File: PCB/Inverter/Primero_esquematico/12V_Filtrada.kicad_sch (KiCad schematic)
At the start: 11 parts, among them U1 TPS259621DDAT

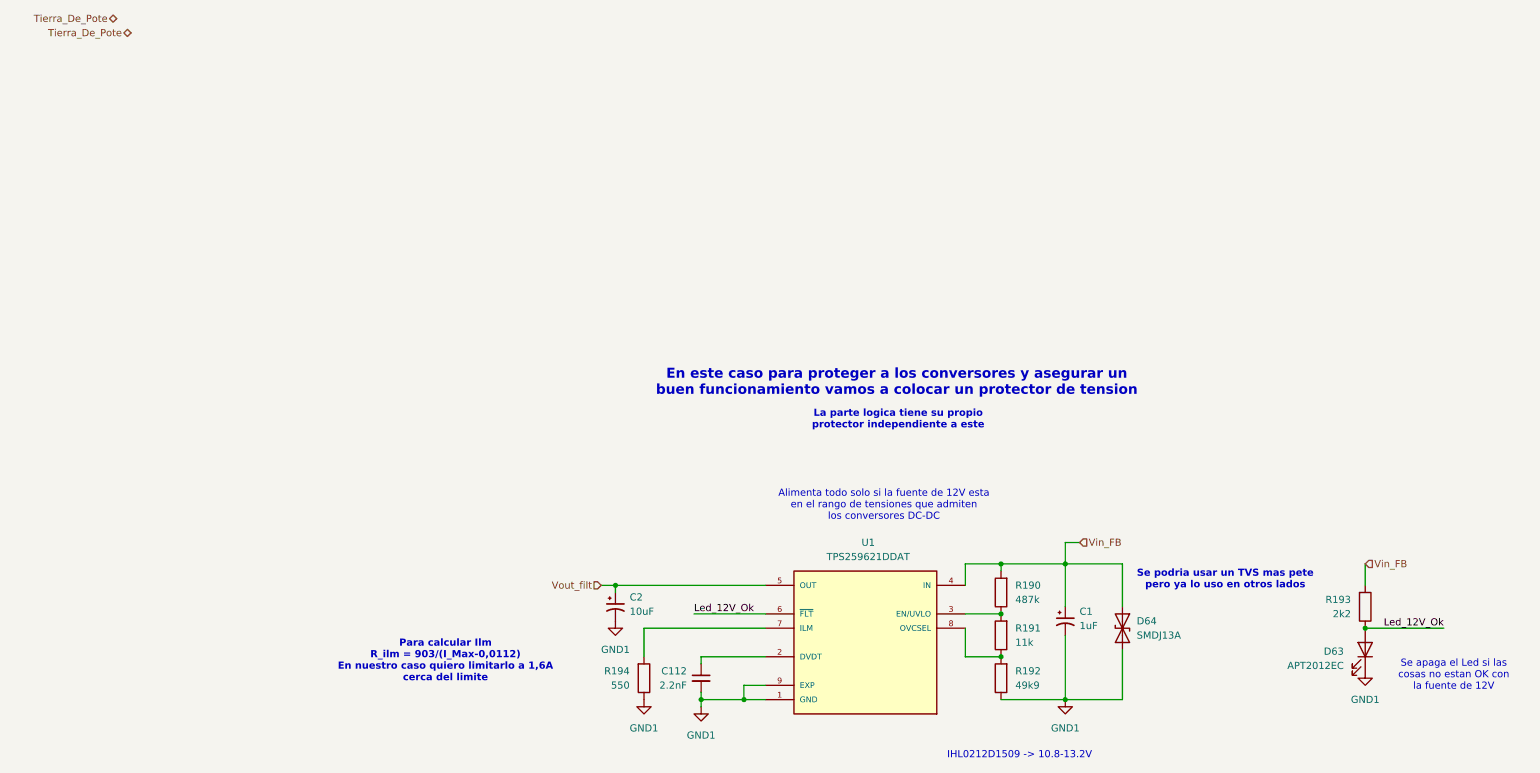
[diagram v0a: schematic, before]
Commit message: Un par de cosas q corregi del ERC pero sigue mal
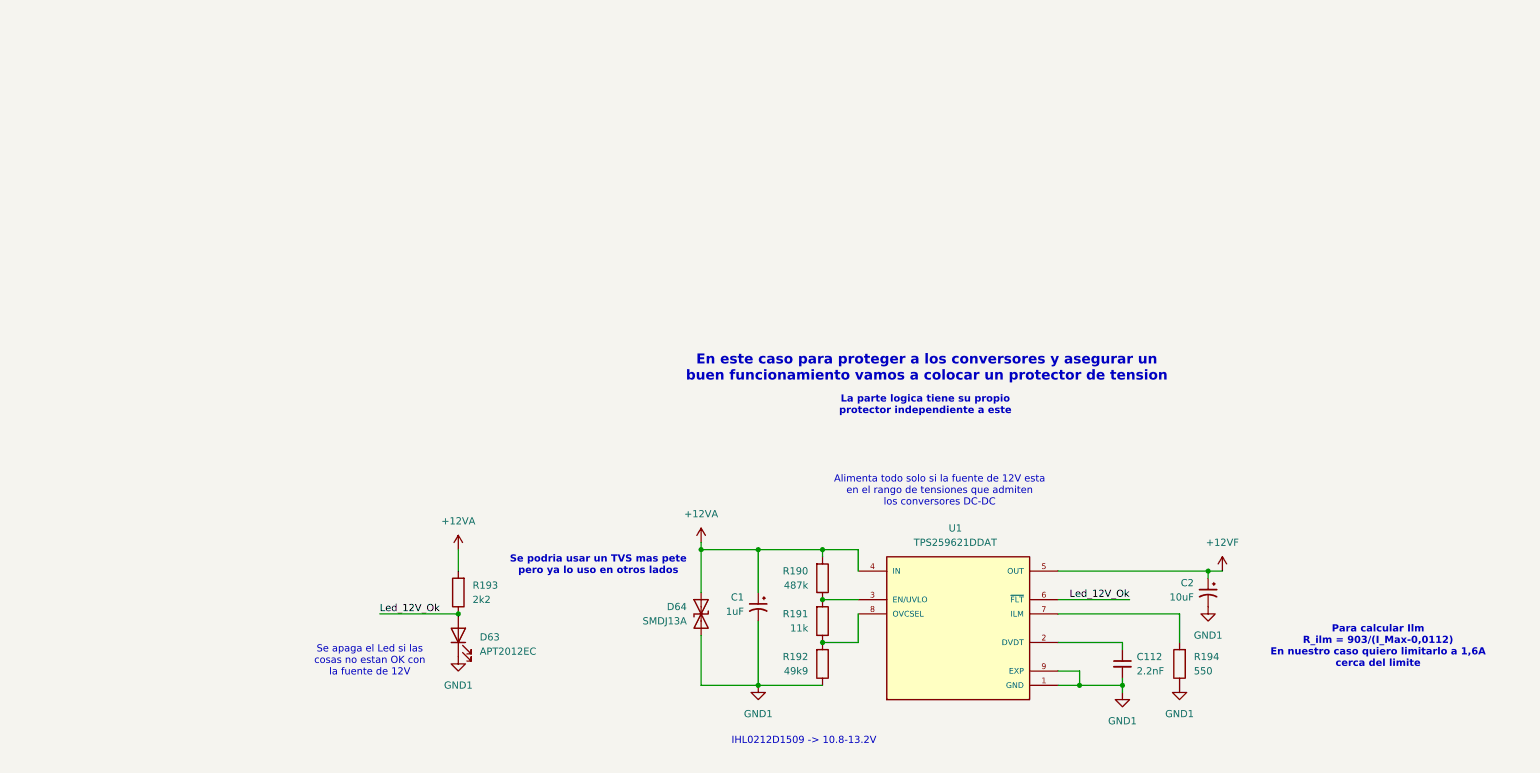
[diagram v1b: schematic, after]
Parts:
- U1: footprint Snapeda:IC_TPS259621DDAT -> TPS259621DDAT:IC_TPS259621DDAT
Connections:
- net Vin_FB renamed +12VA
- net Vout_filt renamed +12VF
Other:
- moved on the sheet: C1, C112, C2, D63, D64, R190, R191, R192, R193, R194, U1

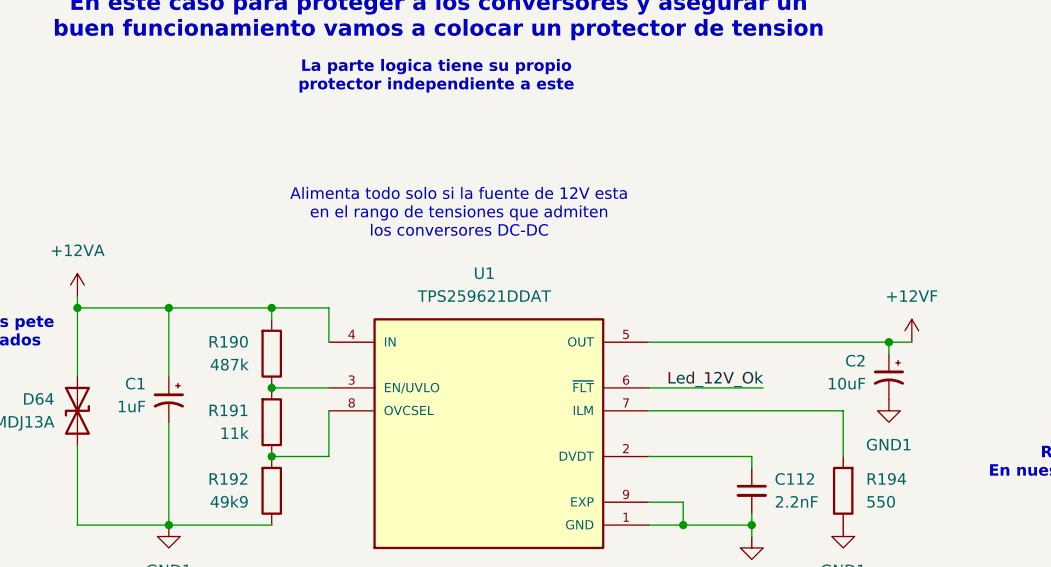
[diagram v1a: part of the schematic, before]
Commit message: Esquematico Listo
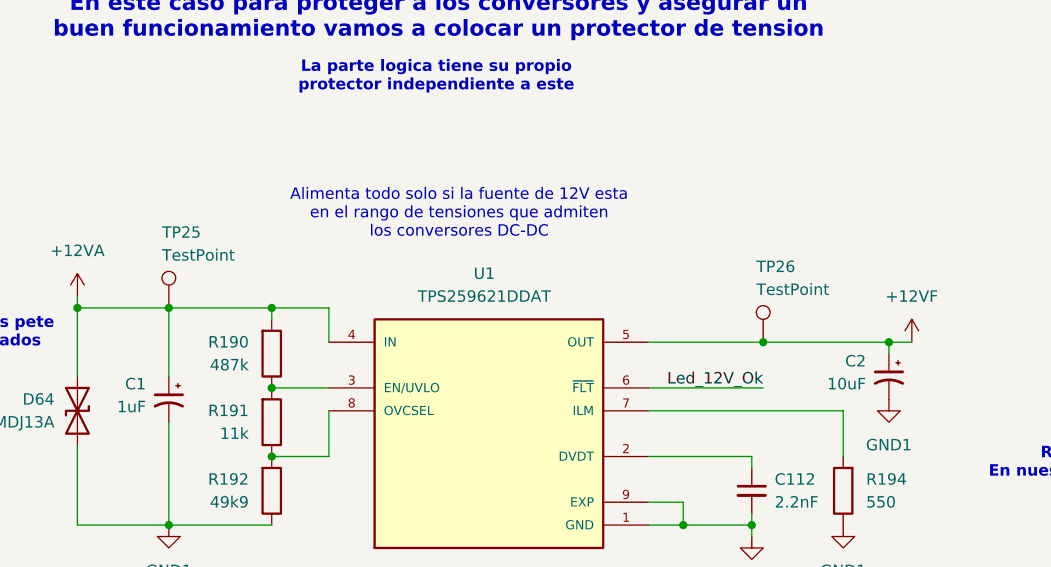
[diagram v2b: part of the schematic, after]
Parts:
- added TP25, TP26: TestPoint, TestPoint:TestPoint_Pad_D2.0mm, symbol Connector:TestPoint
- U1: footprint TPS259621DDAT:IC_TPS259621DDAT -> Snapeda:IC_TPS259621DDAT
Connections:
- net +12VA: now also TP25.1
- net +12VF: now also TP26.1
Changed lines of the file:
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@@
+	)
+	(junction
+		(at 195.58 99.06)
+		(diameter 0)
+		(color 0 0 0 0)
 	)
 	(junction
@@
 	(wire
 		(pts
-			(xy 209.55 99.06) (xy 182.88 99.06)
+			(xy 195.58 99.06) (xy 182.88 99.06)
+		)
+		(stroke
+			(width 0)
+			(type default)
+		)
+	)
+	(wire
+		(pts
+			(xy 209.55 99.06) (xy 195.58 99.06)
 		)
 		(stroke
@@
 				(path "/d930f486-f6ac-489c-907e-47f2cb34cf04/d101e913-ebd1-4e08-b728-82218f47123b/3145a225-26ad-4004-be15-8a1076c951ad"
 					(reference "R194")
+					(unit 1)
+				)
+			)
+		)
+	)
+	(symbol
+		(lib_id "Connector:TestPoint")
+		(at 129.54 95.25 0)
+		(unit 1)
+		(body_style 1)
+		(exclude_from_sim no)
+		(in_bom yes)
+		(on_board yes)
+		(in_pos_files yes)
+		(dnp no)
+		(property "Reference" "TP25"
+			(at 128.778 86.868 0)
+			(show_name no)
+			(do_not_autoplace no)
+			(effects
+				(font
+					(size 1.27 1.27)
+				)
+				(justify left)
+			)
+		)
+		(property "Value" "TestPoint"
+			(at 128.778 89.408 0)
+			(show_name no)
+			(do_not_autoplace no)
+			(effects
+				(font
+					(size 1.27 1.27)
+				)
+				(justify left)
+			)
+		)
+		(property "Footprint" "TestPoint:TestPoint_Pad_D2.0mm"
+			(at 134.62 95.25 0)
+			(hide yes)
+			(show_name no)
+			(do_not_autoplace no)
+			(effects
+				(font
+					(size 1.27 1.27)
+				)
+			)
+		)
+		(property "Datasheet" ""
+			(at 134.62 95.25 0)
+			(hide yes)
+			(show_name no)
+			(do_not_autoplace no)
+			(effects
+				(font
+					(size 1.27 1.27)
+				)
+			)
+		)
+		(property "Description" "test point"
+			(at 129.54 95.25 0)
+			(hide yes)
+			(show_name no)
+			(do_not_autoplace no)
+			(effects
+				(font
+					(size 1.27 1.27)
+				)
+			)
+		)
+		(pin "1"
+		)
+		(instances
+			(project "Primero_esquematico"
+				(path "/d930f486-f6ac-489c-907e-47f2cb34cf04/d101e913-ebd1-4e08-b728-82218f47123b/3145a225-26ad-4004-be15-8a1076c951ad"
+					(reference "TP25")
 					(unit 1)
 				)
@@
 			)
 		)
-		(property "Footprint" "TPS259621DDAT:IC_TPS259621DDAT"
+		(property "Footprint" "Snapeda:IC_TPS259621DDAT"
 			(at 165.1 64.77 0)
 			(hide yes)
@@
 					(unit 1)
 				)
+			)
+		)
+	)
+	(symbol
+		(lib_id "Connector:TestPoint")
+		(at 195.58 99.06 0)
+		(unit 1)
+		(body_style 1)
+		(exclude_from_sim no)
+		(in_bom yes)
+		(on_board yes)
+		(in_pos_files yes)
+		(dnp no)
+		(property "Reference" "TP26"
+			(at 194.818 90.678 0)
+			(show_name no)
+			(do_not_autoplace no)
+			(effects
+				(font
+					(size 1.27 1.27)
+				)
+				(justify left)
+			)
+		)
+		(property "Value" "TestPoint"
+			(at 194.818 93.218 0)
+			(show_name no)
+			(do_not_autoplace no)
+			(effects
+				(font
+					(size 1.27 1.27)
+				)
+				(justify left)
+			)
+		)
+		(property "Footprint" "TestPoint:TestPoint_Pad_D2.0mm"
+			(at 200.66 99.06 0)
+			(hide yes)
+			(show_name no)
+			(do_not_autoplace no)
+			(effects
+				(font
+					(size 1.27 1.27)
+				)
+			)
+		)
+		(property "Datasheet" ""
+			(at 200.66 99.06 0)
+			(hide yes)
+			(show_name no)
+			(do_not_autoplace no)
+			(effects
+				(font
+					(size 1.27 1.27)
+				)
+			)
+		)
+		(property "Description" "test point"
+			(at 195.58 99.06 0)
+			(hide yes)
+			(show_name no)
+			(do_not_autoplace no)
+			(effects
+				(font
+					(size 1.27 1.27)
+				)
+			)
+		)
+		(pin "1"
+		)
+		(instances
+			(project "Primero_esquematico"
+				(path "/d930f486-f6ac-489c-907e-47f2cb34cf04/d101e913-ebd1-4e08-b728-82218f47123b/3145a225-26ad-4004-be15-8a1076c951ad"
+					(reference "TP26")
+					(unit 1)
+				)

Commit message: Un par de cosas mas
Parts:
- C1: value 1uF -> 10uF
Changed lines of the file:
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@@
 		(in_pos_files yes)
 		(dnp no)
-		(fields_autoplaced yes)
 		(property "Reference" "C1"
-			(at 127 103.7081 0)
+			(at 124.46 104.902 0)
 			(show_name no)
 			(do_not_autoplace no)
@@
 					(size 1.27 1.27)
 				)
-				(justify left)
+				(justify right)
 			)
 		)
-		(property "Value" "1uF"
-			(at 127 106.2481 0)
+		(property "Value" "10uF"
+			(at 128.524 107.95 0)
 			(show_name no)
 			(do_not_autoplace no)

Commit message: correcciones
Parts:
- TP1: renamed from TP25; footprint TestPoint:TestPoint_Pad_D2.0mm -> TestPoint:TestPoint_Pad_D1.0mm
- TP2: renamed from TP26; footprint TestPoint:TestPoint_Pad_D2.0mm -> TestPoint:TestPoint_Pad_D1.0mm
- renumbered C112 to C2, C2 to C3, D63 to D1, D64 to D2, R193 to R1, R190 to R2, R191 to R3, R192 to R4, R194 to R5

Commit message: Algunos cambios
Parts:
- removed C3: 10uF, Capacitor_SMD:C_0805_2012Metric, symbol Device:C_Polarized_Small_US
- removed D2: SMDJ13A, Diode_SMD:D_SMC, symbol Device:D_TVS
- added C153: 220uF, Snapeda:WCAP-PSLC_8X11.7_DXL_, symbol Snapeda:WCAP-PSLC_8X11.7
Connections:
- net +12VF: now also C153.1
- net GND1: now also C153.2
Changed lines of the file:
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@@
 	(text "Para calcular Ilm\nR_ilm = 903/(I_Max-0,0112)\nEn nuestro caso quiero limitarlo a 1,6A\ncerca del limite"
 		(exclude_from_sim no)
-		(at 239.776 112.522 0)
+		(at 234.696 115.824 0)
 		(effects
 			(font
@@
 	)
 	(junction
-		(at 119.38 95.25)
-		(diameter 0)
-		(color 0 0 0 0)
-	)
-	(junction
 		(at 194.31 119.38)
 		(diameter 0)
@@
 	(wire
 		(pts
-			(xy 119.38 110.49) (xy 119.38 119.38)
-		)
-		(stroke
-			(width 0)
-			(type default)
-		)
-	)
-	(wire
-		(pts
 			(xy 147.32 104.14) (xy 140.97 104.14)
 		)
@@
 		(pts
 			(xy 76.2 106.68) (xy 62.23 106.68)
-		)
-		(stroke
-			(width 0)
-			(type default)
-		)
-	)
-	(wire
-		(pts
-			(xy 119.38 102.87) (xy 119.38 95.25)
-		)
-		(stroke
-			(width 0)
-			(type default)
-		)
-	)
-	(wire
-		(pts
-			(xy 119.38 119.38) (xy 129.54 119.38)
 		)
 		(stroke
@@
 	)
 	(symbol
-		(lib_id "Device:D_TVS")
-		(at 119.38 106.68 90)
-		(mirror x)
-		(unit 1)
-		(body_style 1)
-		(exclude_from_sim no)
-		(in_bom yes)
-		(on_board yes)
-		(in_pos_files yes)
-		(dnp no)
-		(fields_autoplaced yes)
-		(property "Reference" "D2"
-			(at 116.84 105.4099 90)
-			(show_name no)
-			(do_not_autoplace no)
-			(effects
-				(font
-					(size 1.27 1.27)
-				)
-				(justify left)
-			)
-		)
-		(property "Value" "SMDJ13A"
-			(at 116.84 107.9499 90)
-			(show_name no)
-			(do_not_autoplace no)
-			(effects
-				(font
-					(size 1.27 1.27)
-				)
-				(justify left)
-			)
-		)
-		(property "Footprint" "Diode_SMD:D_SMC"
-			(at 119.38 106.68 0)
-			(hide yes)
-			(show_name no)
-			(do_not_autoplace no)
-			(effects
-				(font
-					(size 1.27 1.27)
-				)
-			)
-		)
-		(property "Datasheet" "https://www.ruilon.com.cn/Uploads/pdf/smdj%20series(3000w,5v_440v).pdf"
-			(at 119.38 106.68 0)
-			(hide yes)
-			(show_name no)
-			(do_not_autoplace no)
-			(effects
-				(font
-					(size 1.27 1.27)
-				)
-			)
-		)
-		(property "Description" "Bidirectional transient-voltage-suppression diode"
-			(at 119.38 106.68 0)
-			(hide yes)
-			(show_name no)
-			(do_not_autoplace no)
-			(effects
-				(font
-					(size 1.27 1.27)
-				)
-			)
-		)
-		(property "Compra" "https://www.digikey.com/en/products/detail/shenzhen-ruilongyuan-electronics-co-ltd/smdj13a/24815173"
-			(at 119.38 106.68 0)
-			(hide yes)
-			(show_name no)
-			(do_not_autoplace no)
-			(effects
-				(font
-					(size 1.27 1.27)
-				)
-			)
-		)
-		(property "Description_1" ""
-			(at 119.38 106.68 90)
-			(hide yes)
-			(show_name no)
-			(do_not_autoplace no)
-			(effects
-				(font
-					(size 1.27 1.27)
-				)
-			)
-		)
-		(pin "2"
-		)
-		(pin "1"
-		)
-		(instances
-			(project "Primero_esquematico"
-				(path "/d930f486-f6ac-489c-907e-47f2cb34cf04/d101e913-ebd1-4e08-b728-82218f47123b/3145a225-26ad-4004-be15-8a1076c951ad"
-					(reference "D2")
-					(unit 1)
-				)
-			)
-		)
-	)
-	(symbol
 		(lib_id "Device:R")
 		(at 140.97 107.95 0)
@@
 	)
 	(symbol
-		(lib_id "Device:C_Polarized_Small_US")
-		(at 209.55 102.87 0)
-		(mirror y)
-		(unit 1)
-		(body_style 1)
-		(exclude_from_sim no)
-		(in_bom yes)
-		(on_board yes)
-		(in_pos_files yes)
-		(dnp no)
-		(fields_autoplaced yes)
-		(property "Reference" "C3"
-			(at 207.01 101.1681 0)
-			(show_name no)
-			(do_not_autoplace no)
-			(effects
-				(font
-					(size 1.27 1.27)
-				)
-				(justify left)
-			)
-		)
-		(property "Value" "10uF"
-			(at 207.01 103.7081 0)
-			(show_name no)
-			(do_not_autoplace no)
-			(effects
-				(font
-					(size 1.27 1.27)
-				)
-				(justify left)
-			)
-		)
-		(property "Footprint" "Capacitor_SMD:C_0805_2012Metric"
-			(at 209.55 102.87 0)
-			(hide yes)
-			(show_name no)
-			(do_not_autoplace no)
-			(effects
-				(font
-					(size 1.27 1.27)
-				)
-			)
-		)
-		(property "Datasheet" ""
-			(at 209.55 102.87 0)
-			(hide yes)
-			(show_name no)
-			(do_not_autoplace no)
-			(effects
-				(font
-					(size 1.27 1.27)
-				)
-			)
-		)
-		(property "Description" "Polarized capacitor, small US symbol"
-			(at 209.55 102.87 0)
-			(hide yes)
-			(show_name no)
-			(do_not_autoplace no)
-			(effects
-				(font
-					(size 1.27 1.27)
-				)
-			)
-		)
-		(property "Description_1" ""
-			(at 209.55 102.87 0)
-			(hide yes)
-			(show_name no)
-			(do_not_autoplace no)
-			(effects
-				(font
-					(size 1.27 1.27)
-				)
-			)
-		)
-		(pin "2"
-		)
-		(pin "1"
-		)
-		(instances
-			(project "Primero_esquematico"
-				(path "/d930f486-f6ac-489c-907e-47f2cb34cf04/d101e913-ebd1-4e08-b728-82218f47123b/3145a225-26ad-4004-be15-8a1076c951ad"
-					(reference "C3")
-					(unit 1)
-				)
-			)
-		)
-	)
-	(symbol
 		(lib_id "Device:C_Small")
 		(at 194.31 115.57 0)
@@
 	)
 	(symbol
+		(lib_id "Snapeda:WCAP-PSLC_8X11.7")
+		(at 209.55 105.41 90)
+		(unit 1)
+		(body_style 1)
+		(exclude_from_sim no)
+		(in_bom yes)
+		(on_board yes)
+		(in_pos_files yes)
+		(dnp no)
+		(fields_autoplaced yes)
+		(property "Reference" "C153"
+			(at 213.36 101.903 90)
+			(show_name no)
+			(do_not_autoplace no)
+			(effects
+				(font
+					(size 1.27 1.27)
+				)
+				(justify right)
+			)
+		)
+		(property "Value" "220uF"
+			(at 213.36 104.443 90)
+			(show_name no)
+			(do_not_autoplace no)
+			(effects
+				(font
+					(size 1.27 1.27)
+				)
+				(justify right)
+			)
+		)
+		(property "Footprint" "Snapeda:WCAP-PSLC_8X11.7_DXL_"
+			(at 205.74 100.6332 90)
+			(hide yes)
+			(show_name no)
+			(do_not_autoplace no)
+			(effects
+				(font
+					(size 1.27 1.27)
+				)
+				(justify left)
+			)
+		)
+		(property "Datasheet" "https://www.we-online.com/components/products/datasheet/875075355002.pdf"
+			(at 209.55 105.41 0)
+			(hide yes)
+			(show_name no)
+			(do_not_autoplace no)
+			(effects
+				(font
+					(size 1.27 1.27)
+				)
+			)
+		)
+		(property "Description" "WCAP-PSLC_8X11.7"
+			(at 209.55 105.41 0)
+			(hide yes)
+			(show_name no)
+			(do_not_autoplace no)
+			(effects
+				(font
+					(size 1.27 1.27)
+				)
+			)
+		)
+		(property "Compra" "https://www.digikey.com/es/products/detail/w%C3%BCrth-elektronik/875075355002/5147653"
+			(at 209.55 105.41 90)
+			(hide yes)
+			(show_name no)
+			(do_not_autoplace no)
+			(effects
+				(font
+					(size 1.27 1.27)
+				)
+			)
+		)
+		(pin "1"
+		)
+		(pin "2"
+		)
+		(instances
+			(project "Primero_esquematico"
+				(path "/d930f486-f6ac-489c-907e-47f2cb34cf04/d101e913-ebd1-4e08-b728-82218f47123b/3145a225-26ad-4004-be15-8a1076c951ad"
+					(reference "C153")
+					(unit 1)
+				)
+			)
+		)
+	)
+	(symbol
 		(lib_id "power:+12V")
 		(at 119.38 93.98 0)
@@
 	(symbol
 		(lib_id "power:GND1")
-		(at 209.55 105.41 0)
+		(at 209.55 107.95 0)
 		(mirror y)
 		(unit 1)
@@
 		(in_pos_files yes)
 		(dnp no)
-		(fields_autoplaced yes)
 		(property "Reference" "#PWR07"
-			(at 209.55 111.76 0)
+			(at 209.55 114.3 0)
 			(hide yes)
 			(show_name no)
@@
 		)
 		(property "Value" "GND1"
-			(at 209.55 110.49 0)
+			(at 213.614 110.744 0)
 			(show_name no)
 			(do_not_autoplace no)
@@
 		)
 		(property "Footprint" ""
-			(at 209.55 105.41 0)
+			(at 209.55 107.95 0)
 			(hide yes)
 			(show_name no)
@@
 		)
 		(property "Datasheet" ""
-			(at 209.55 105.41 0)
+			(at 209.55 107.95 0)
 			(hide yes)
 			(show_name no)
@@
 		)
 		(property "Description" "Power symbol creates a global label with name \"GND1\" , ground"
-			(at 209.55 105.41 0)
-			(hide yes)
-			(show_name no)
+			(at 209.55 107.95 0)
+			(hide yes)
+			(show_name no)
